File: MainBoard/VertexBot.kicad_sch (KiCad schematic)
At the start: 47 parts, among them J1 Battery, J4 Left Motor, J5 Right Motor, J6 Led Strip, Q1 BSS138, Q2 BSS138, Q3 BSS138, SW1 SW_SPST, U1 DRV8830DGQR, U10 MAX4466, U11 MAX4466, U12 ESP32-S3-CAM-B, U13 ESP32-S3-CAM-A, U14 MAX98357A, U2 DRV8830DGQR, U3 S13V30F5, U5 INMP441, U6 0.96 INCH OLED, U7 DRV5033AJxLPG, U8 DRV5033AJxLPG, U9 MPU 6050

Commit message: Remove junction (accidently added by tool) and adjust colors
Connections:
- net GND: no longer J1.2 (Pin_2), SW1.1 (A), TP1.1
- new net: J1.2 (Pin_2), SW1.1 (A), TP1.1
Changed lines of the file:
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@@
 	)
 	(junction
-		(at 39.37 90.17)
+		(at 116.84 68.58)
+		(diameter 0)
+		(color 0 0 255 1)
+	)
+	(junction
+		(at 217.17 118.11)
+		(diameter 0)
+		(color 0 0 255 1)
+	)
+	(junction
+		(at 127 113.03)
+		(diameter 0)
+		(color 255 153 0 1)
+	)
+	(junction
+		(at 55.88 46.99)
+		(diameter 0)
+		(color 194 0 0 1)
+	)
+	(junction
+		(at 226.06 39.37)
 		(diameter 0)
 		(color 0 0 0 0)
 	)
 	(junction
-		(at 116.84 68.58)
+		(at 31.75 162.56)
 		(diameter 0)
 		(color 0 0 255 1)
 	)
 	(junction
-		(at 217.17 118.11)
+		(at 116.84 57.15)
 		(diameter 0)
 		(color 0 0 255 1)
 	)
 	(junction
-		(at 127 113.03)
+		(at 114.3 68.58)
+		(diameter 0)
+		(color 0 0 255 1)
+	)
+	(junction
+		(at 96.52 68.58)
+		(diameter 0)
+		(color 0 0 255 1)
+	)
+	(junction
+		(at 160.02 69.85)
+		(diameter 0)
+		(color 194 0 0 1)
+	)
+	(junction
+		(at 39.37 68.58)
+		(diameter 0)
+		(color 0 0 255 1)
+	)
+	(junction
+		(at 29.21 139.7)
 		(diameter 0)
 		(color 255 153 0 1)
 	)
 	(junction
-		(at 55.88 46.99)
+		(at 123.19 69.85)
 		(diameter 0)
 		(color 194 0 0 1)
 	)
 	(junction
-		(at 226.06 39.37)
+		(at 88.9 100.33)
+		(diameter 0)
+		(color 194 0 0 1)
+	)
+	(junction
+		(at 139.7 113.03)
+		(diameter 0)
+		(color 255 153 0 1)
+	)
+	(junction
+		(at 237.49 60.96)
+		(diameter 0)
+		(color 0 0 255 1)
+	)
+	(junction
+		(at 39.37 124.46)
 		(diameter 0)
 		(color 0 0 0 0)
 	)
 	(junction
-		(at 31.75 162.56)
+		(at 118.11 113.03)
+		(diameter 0)
+		(color 255 153 0 1)
+	)
+	(junction
+		(at 166.37 68.58)
 		(diameter 0)
 		(color 0 0 255 1)
-	)
-	(junction
-		(at 116.84 57.15)
-		(diameter 0)
-		(color 0 0 255 1)
-	)
-	(junction
-		(at 114.3 68.58)
-		(diameter 0)
-		(color 0 0 255 1)
-	)
-	(junction
-		(at 96.52 68.58)
-		(diameter 0)
-		(color 0 0 255 1)
-	)
-	(junction
-		(at 160.02 69.85)
-		(diameter 0)
-		(color 194 0 0 1)
-	)
-	(junction
-		(at 39.37 68.58)
-		(diameter 0)
-		(color 0 0 255 1)
-	)
-	(junction
-		(at 29.21 139.7)
-		(diameter 0)
-		(color 255 153 0 1)
-	)
-	(junction
-		(at 123.19 69.85)
-		(diameter 0)
-		(color 0 0 0 0)
-	)
-	(junction
-		(at 88.9 100.33)
-		(diameter 0)
-		(color 194 0 0 1)
-	)
-	(junction
-		(at 139.7 113.03)
-		(diameter 0)
-		(color 255 153 0 1)
-	)
-	(junction
-		(at 237.49 60.96)
-		(diameter 0)
-		(color 0 0 255 1)
-	)
-	(junction
-		(at 39.37 124.46)
-		(diameter 0)
-		(color 0 0 0 0)
-	)
-	(junction
-		(at 118.11 113.03)
-		(diameter 0)
-		(color 255 153 0 1)
-	)
-	(junction
-		(at 166.37 68.58)
-		(diameter 0)
-		(color 0 0 0 0)
 	)
 	(junction
@@
 	(wire
 		(pts
-			(xy 39.37 90.17) (xy 59.69 90.17)
-		)
-		(stroke
-			(width 0)
-			(type default)
-		)
-	)
-	(wire
-		(pts
 			(xy 165.1 115.57) (xy 165.1 139.7)
 		)
@@
 	(wire
 		(pts
-			(xy 39.37 90.17) (xy 39.37 124.46)
+			(xy 39.37 87.63) (xy 39.37 124.46)
 		)
 		(stroke
@@
 	(wire
 		(pts
-			(xy 39.37 87.63) (xy 39.37 90.17)
-		)
-		(stroke
-			(width 0)
-			(type default)
-			(color 0 0 255 1)
-		)
-	)
-	(wire
-		(pts
 			(xy 247.65 149.86) (xy 82.55 149.86)
 		)
@@
 	(wire
 		(pts
-			(xy 36.83 90.17) (xy 39.37 90.17)
-		)
-		(stroke
+			(xy 36.83 90.17) (xy 59.69 90.17)
+		)
+		(stroke

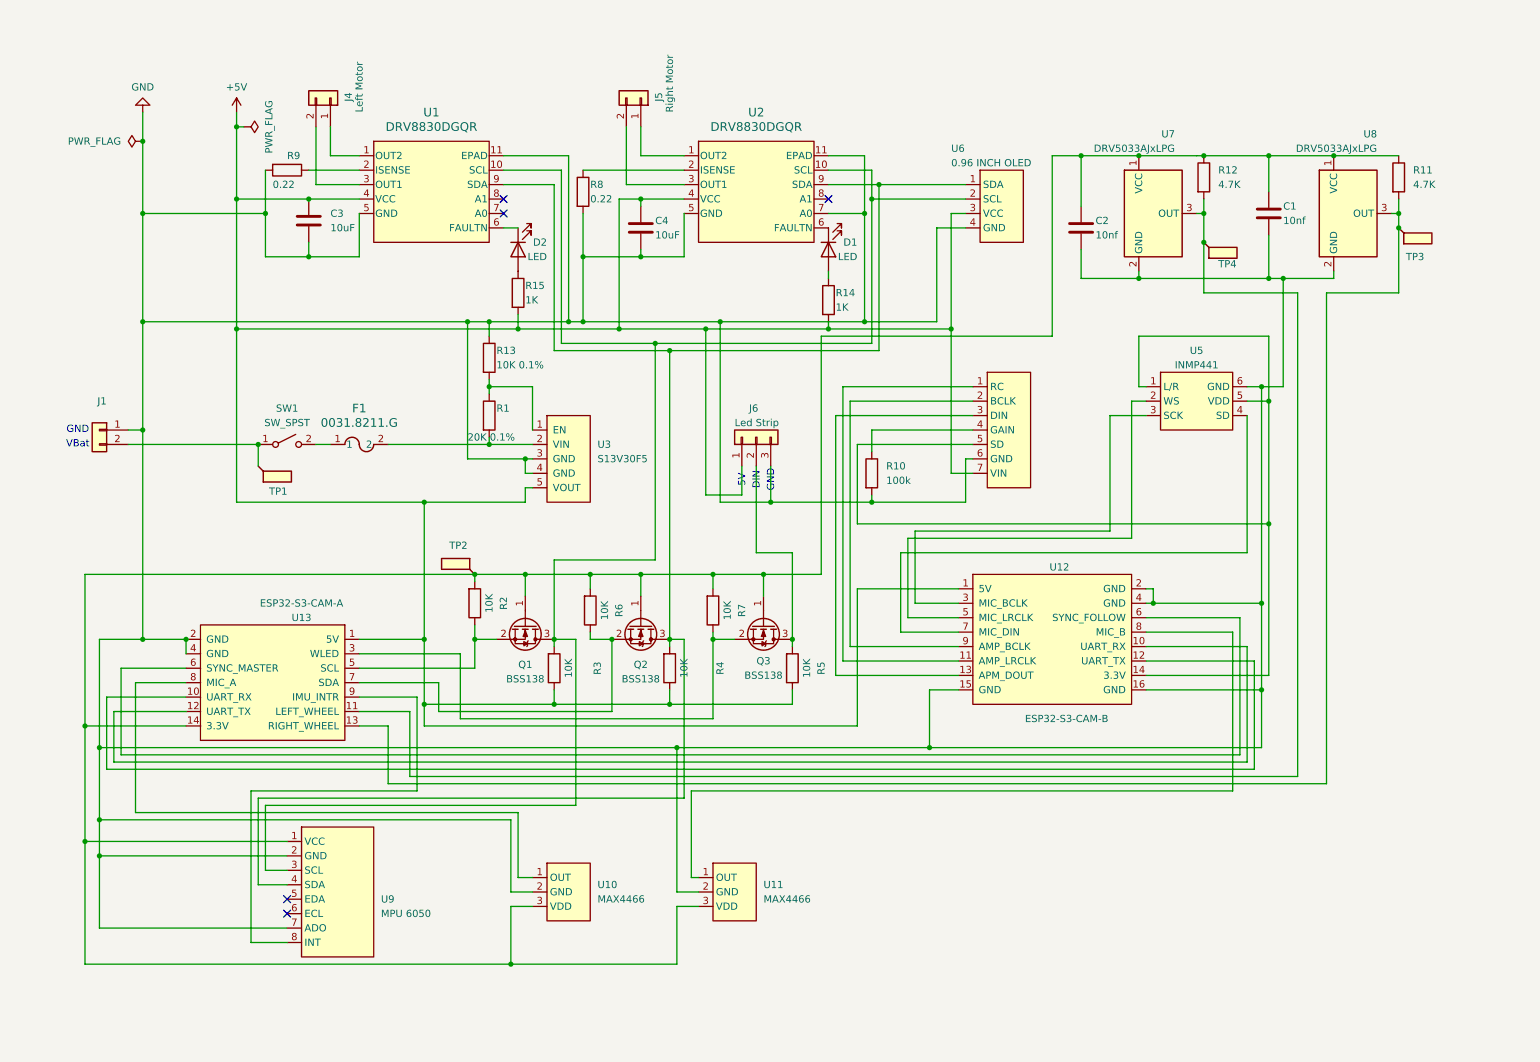
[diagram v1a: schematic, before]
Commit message: - Relayed schematic with better modular approach (Global labels usage) - Edge cut so that now backboards are facing to the sides, central rectangular hole rotated by 90 - Some fooprints DRC'ed and fixed (more to come)
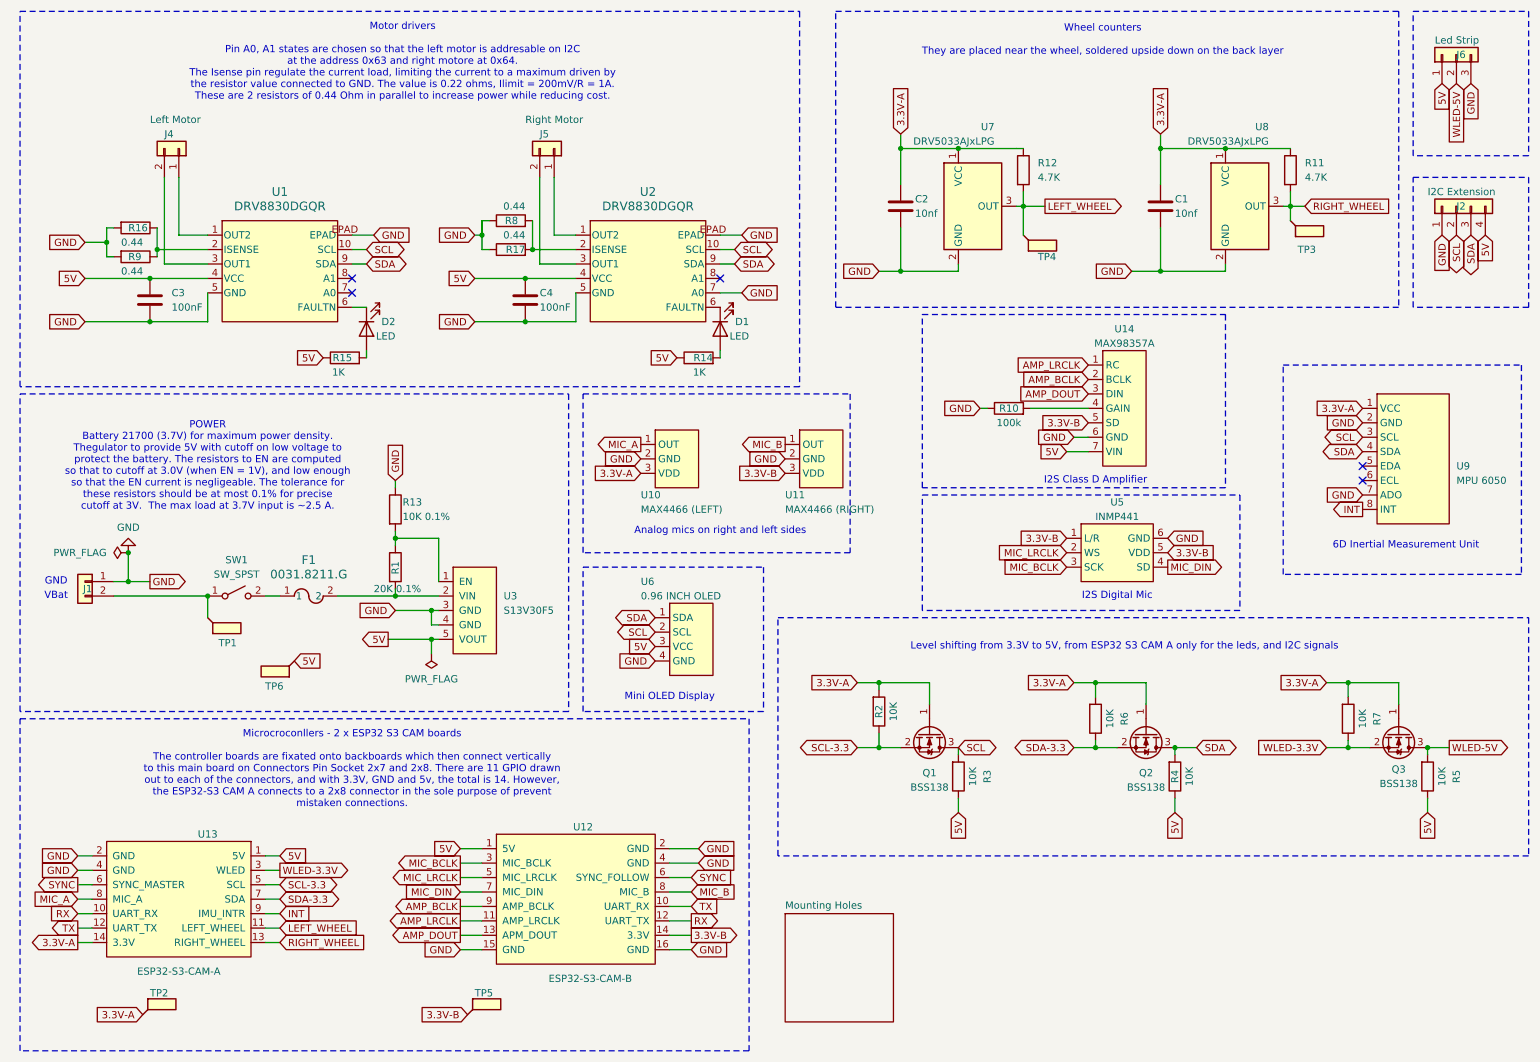
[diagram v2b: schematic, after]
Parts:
- added J2: I2C Extension, Connector_JST:JST_XH_S3B-XH-A-1_1x03_P2.50mm_Horizontal, symbol Connector_Generic:Conn_01x04
- added R16, R17: 0.44, Resistor_SMD:R_0603_1608Metric, symbol Device:R
- added TP5, TP6: TestPoint_Flag, TestPoint:TestPoint_Pad_3.0x3.0mm, symbol Connector:TestPoint_Flag
- C1: footprint Capacitor_SMD:C_0201_0603Metric -> Capacitor_SMD:C_0603_1608Metric
- C2: footprint Capacitor_SMD:C_0201_0603Metric -> Capacitor_SMD:C_0603_1608Metric_Pad1.08x0.95mm_HandSolder
- C3, C4: value 10uF -> 100nF; footprint Capacitor_SMD:C_0201_0603Metric -> Capacitor_SMD:C_0603_1608Metric
- R1, R10, R11, R12, R13, R14, R15, R2, R3, R4, R5, R6, R7: footprint Resistor_SMD:R_0201_0603Metric -> Resistor_SMD:R_0603_1608Metric
- R8, R9: value 0.22 -> 0.44; footprint Resistor_SMD:R_0201_0603Metric -> Resistor_SMD:R_0603_1608Metric
- U10: value MAX4466 -> MAX4466 (LEFT)
- U11: value MAX4466 -> MAX4466 (RIGHT)
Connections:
- net GND: now also R10.1, R8.1, U1.EPAD, U2.EPAD, J2.1 (Pin_1), R16.2, R17.1; no longer R10.2, R8.2, U1.11 (EPAD), U2.11 (EPAD)
- net 3.3V-A: now reaches C1.1, C2.1, Q1.1 (G), Q2.1 (G), Q3.1 (G), R11.1, R12.1, R2.2, R6.2, R7.2, TP2.1, U10.3 (VDD), U13.14 (3.3V), U7.1 (VCC), U8.1 (VCC), U9.1 (VCC)
- net 3.3V-A: no longer U11.3 (VDD)
- net SCL-3.3: now reaches Q1.2 (S), R2.1, U13.5 (SCL)
- net SCL: now reaches Q1.3 (D), R3.2, U1.10 (SCL), U2.10 (SCL), U6.2 (SCL), U9.3 (SCL)
- net SCL: now also J2.2 (Pin_2)
- net at D2.2 (A): now also R15.2; no longer R15.1
- net SDA-3.3: now reaches Q2.2 (S), R6.1, U13.7 (SDA)
- net SDA: now reaches Q2.3 (D), R4.2, U1.9 (SDA), U2.9 (SDA), U6.1 (SDA), U9.4 (SDA)
- net SDA: now also J2.3 (Pin_3)
- net MIC_A: now reaches U10.1 (OUT), U13.8 (MIC_A)
- net at R9.1, U1.2 (ISENSE): now also R16.1
- net at D1.2 (A): now also R14.2; no longer R14.1
- net INT: now reaches U13.9 (IMU_INTR), U9.8 (INT)
- net at U14.4 (GAIN): now also R10.2; no longer R10.1
- net at U2.2 (ISENSE): now also R8.2, R17.2; no longer R8.1
- net RIGHT_WHEEL: now reaches R11.2, TP3.1, U13.13 (RIGHT_WHEEL), U8.3 (OUT)
- net LEFT_WHEEL: now reaches R12.2, TP4.1, U13.11 (LEFT_WHEEL), U7.3 (OUT)
- net WLED-3.3V: now reaches Q3.2 (S), R7.1, U13.3 (WLED)
- net WLED-5V: now reaches J6.2 (Pin_2), Q3.3 (D), R5.2
- net 3.3V-B: now reaches U12.14 (3.3V), U14.5 (SD), U5.1 (L/R), U5.5 (VDD)
- net 3.3V-B: now also U11.3 (VDD), TP5.1
- net MIC_LRCLK: now reaches U12.5 (MIC_LRCLK), U5.2 (WS)
- net MIC_BCLK: now reaches U12.3 (MIC_BCLK), U5.3 (SCK)
- net MIC_DIN: now reaches U12.7 (MIC_DIN), U5.4 (SD)
- net TX: now reaches U12.10 (UART_RX), U13.12 (UART_TX)
- net AMP_LRCLK: now reaches U12.11 (AMP_LRCLK), U14.1 (RC)
- net RX: now reaches U12.12 (UART_TX), U13.10 (UART_RX)
- net AMP_DOUT: now reaches U12.13 (APM_DOUT), U14.3 (DIN)
- net SYNC: now reaches U12.6 (SYNC_FOLLOW), U13.6 (SYNC_MASTER)
- net MIC_B: now reaches U11.1 (OUT), U12.8 (MIC_B)
- net AMP_BCLK: now reaches U12.9 (AMP_BCLK), U14.2 (BCLK)
- net +5V renamed 5V
- net 5V: now also R14.1, R15.1, J2.4 (Pin_4), TP6.1; no longer R14.2, R15.2
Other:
- added sheet Mounting Holes (MountingHoles.kicad_sch)
- note added: "6D Inertial Measurement Unit"
- note added: "Analog mics on right and left sides"
- note added: "I2S Class D Amplifier"
- note added: "I2S Digital Mic"
- note added: "Level shifting from 3.3V to 5V, from ESP32 S3 CAM A only for the leds, and I2C signals"
- note added: "Microcroconllers - 2 x ESP32 S3 CAM boards The controller boards are fixated onto backboards which then connect vertically to this main board on Connectors Pin Socket 2x7 and 2x8. There are 11 GPIO drawn out to each of the connectors, and with 3.3V, GND and 5v, the total is 14. However, the ESP32-S3 CAM A connects to a 2x8 connector in the sole purpose of prevent mistaken connections."
- note added: "Mini OLED Display"
- note added: "Motor drivers Pin A0, A1 states are chosen so that the left motor is addresable on I2C at the address 0x63 and right motore at 0x64. The Isense pin regulate the current load, limiting the current to a maximum driven by the resistor value connected to GND. The value is 0.22 ohms, Ilimit = 200mV/R = 1A. These are 2 resistors of 0.44 Ohm in parallel to increase power while reducing cost."
- note added: "POWER Battery 21700 (3.7V) for maximum power density. Thegulator to provide 5V with cutoff on low voltage to protect the battery. The resistors to EN are computed so that to cutoff at 3.0V (when EN = 1V), and low enough so that the EN current is negligeable. The tolerance for these resistors should be at most 0.1% for precise cutoff at 3V. The max load at 3.7V input is ~2.5 A."
- note added: "Wheel counters They are placed near the wheel, soldered upside down on the back layer"
- note removed: "5V"
- note removed: "DIN"
- title: Vertex Bot Main Board -> Vertex Bot Main Board (Draft)
- moved on the sheet: C1, C2, C3, C4, D1, D2, F1, J1, J4, J5, J6, Q1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
